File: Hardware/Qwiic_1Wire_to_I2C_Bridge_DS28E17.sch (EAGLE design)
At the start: 20 parts, among them J1 RJ45, J2 RJ45, J3 RJ11, J4 RJ11

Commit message: Update to board
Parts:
- removed JP4: JUMPER-SMT_3_NO_NO-SILK, SparkFun-Jumpers:JUMPER-SMT_3_NO_NO-SILK
- removed U$1: DS28E17, SparkX:DS28E17
- added JP6: JUMPER-SMT_2_NC_PASTE_SILK, SparkFun-Jumpers:JUMPER-SMT_2_NC_PASTE_SILK
- added LOGO1: OSHW-LOGOM, SparkFun-Aesthetics:OSHW-LOGOM
- added U$2, U$3: SPARKX-LOGO5, SparkX:SPARKX-LOGO5
- added U1: DS28E17, SparkX:DS28E17
- JP2: value JUMPER-SMT_2_NO_NO-SILK -> JUMPER-SMT_3_2-NC_PASTE_SILK; device SparkFun-Jumpers:JUMPER-SMT_2_NO_NO-SILK -> SparkFun-Jumpers:JUMPER-SMT_3_2-NC_PASTE_SILK
- R3: value 4.7K -> 4.7k; device SparkFun-Resistors:4.7KOHM-1/10W-1%(0603) -> SparkFun-Resistors:4.7KOHM-0603-1/10W-1%
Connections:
- net 3.3V: now also JP6.2, U1.VCC; no longer JP4.2, U$1.VCC
- net AWAKE: now also U1.AWAKE; no longer U$1.AWAKE
- net BUSY: now also U1.BUSY; no longer U$1.BUSY
- net ED: now also U1.ED; no longer U$1.ED
- net GND: now also U1.!SLEEP, U1.GND; no longer U$1.GND, U$1.SLEEP
- net IO: now also U1.IO, U1.WAKE; no longer U$1.IO, U$1.WAKE
- net N$1: now also U1.REG18; no longer U$1.REG18
- net N$2: now also JP6.1; no longer JP2.1
- net N$3: now also JP2.1; no longer JP4.1
- net N$4: now also JP2.3; no longer JP4.3
- net SCL: now also U1.SCL; no longer U$1.SCL
- net SDA: now also U1.SDA; no longer U$1.SDA
- net XD: now also U1.XD; no longer U$1.XD
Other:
- note added: "1WIRE PTH"
- note added: "1Wire Bus"
- note added: "DS28E17"
- note added: "I2C PTH"
- note added: "JP2 = I2C Pullups Closed by Default"
- note added: "JP6 = 1Wire Pullup Closed by Default"
- note added: "Qwiic I2C ports"
- note added: "X10"
- note removed: "1Wire - IN"
- note removed: "1Wire - OUT"
- moved on the sheet: C1, J1, J2, J3, J4, J5, JP1, JP3, JP5, R1, R2, R3

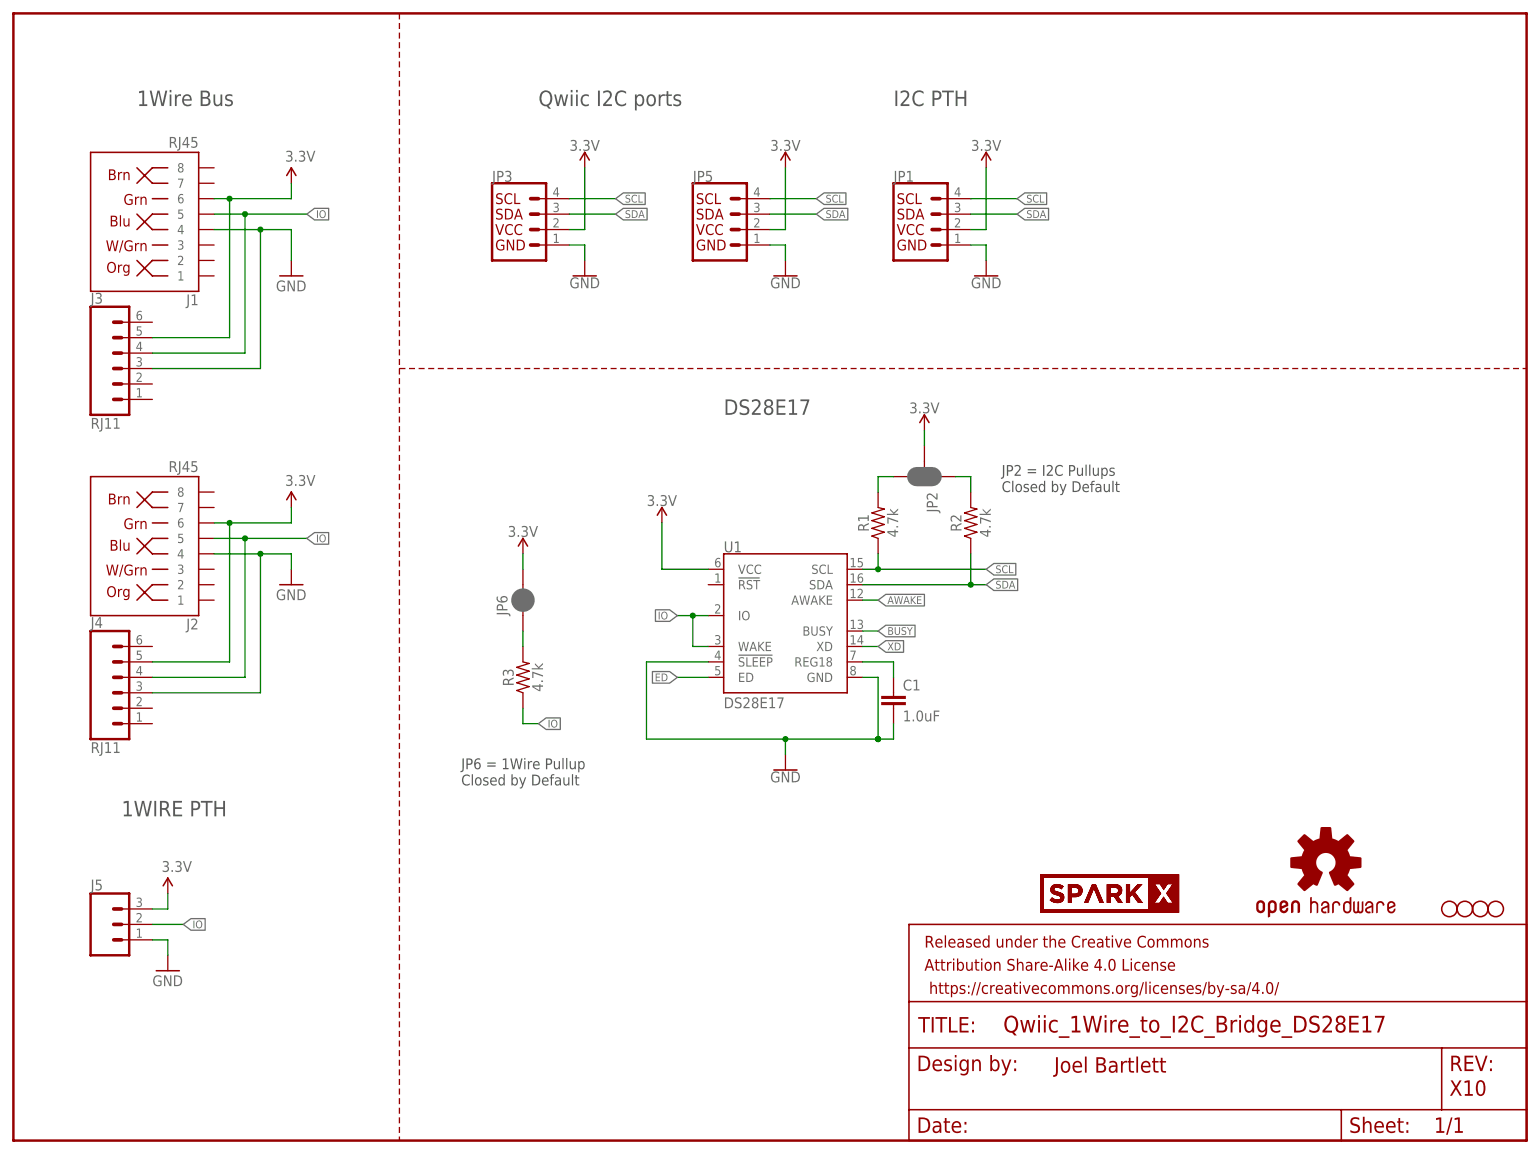
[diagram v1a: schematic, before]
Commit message: Added RJ45/RJ11 footprint. CAM new panel gerbers
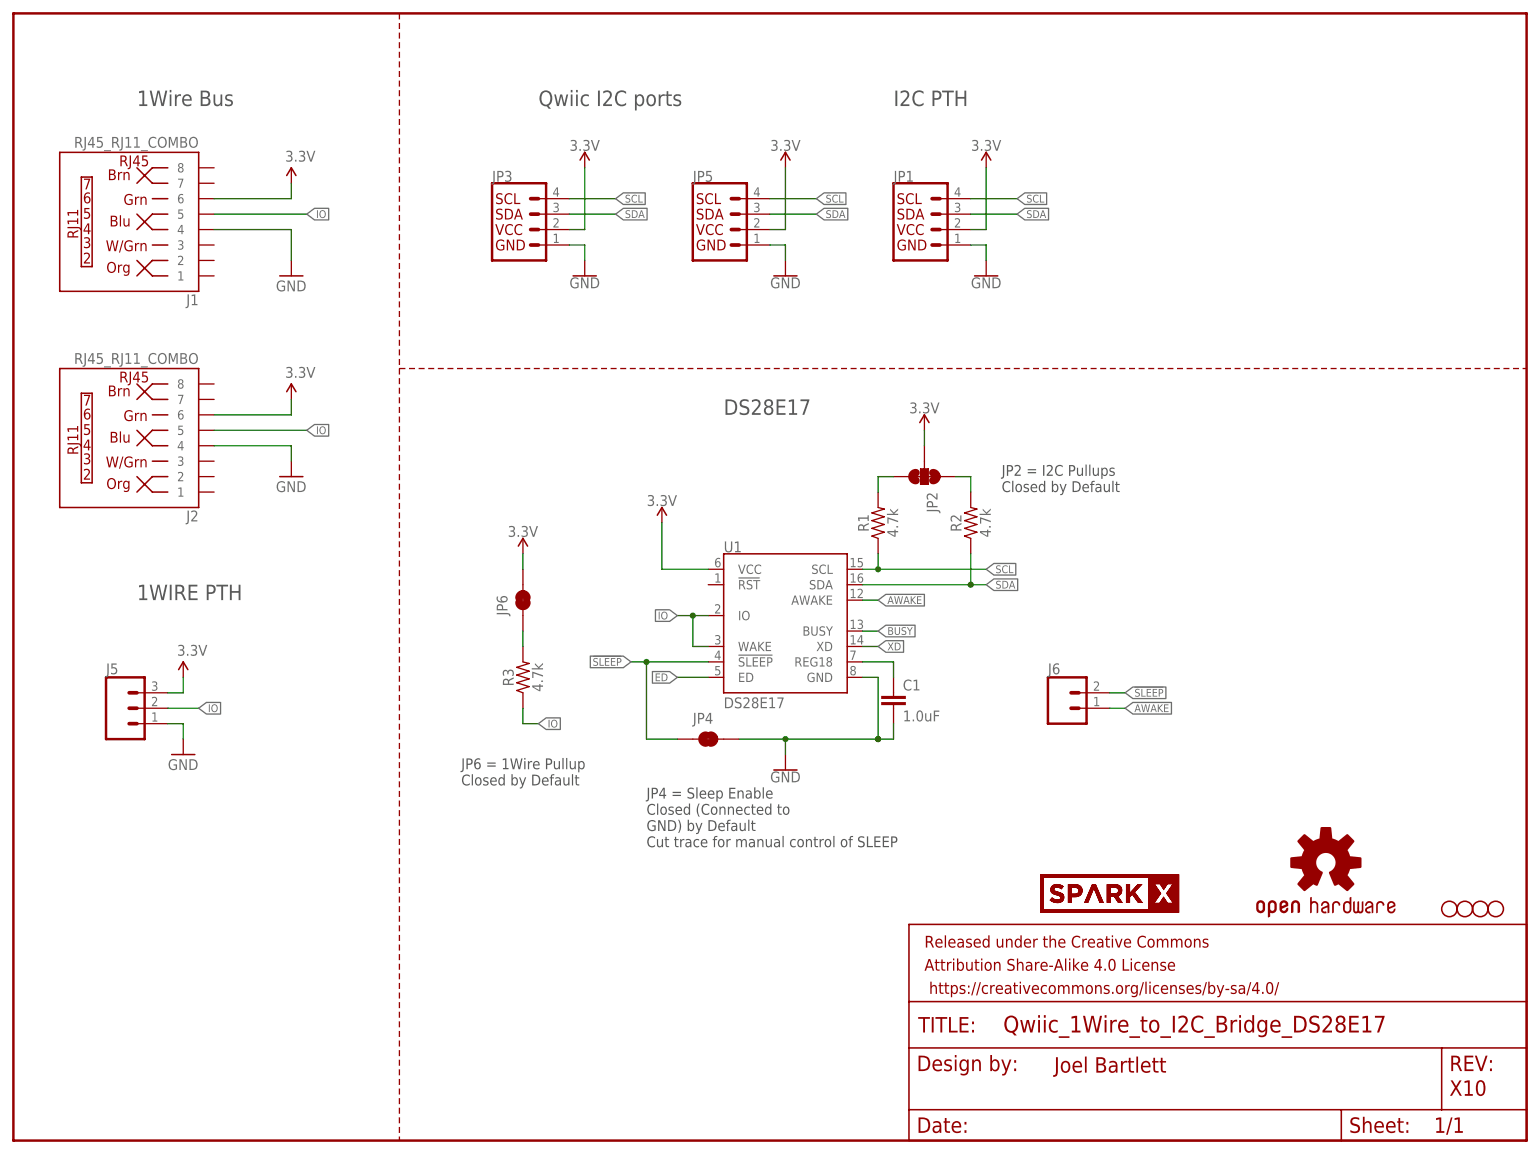
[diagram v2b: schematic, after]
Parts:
- removed J3, J4: RJ11, SparkFun-Connectors:RJ11-6
- added J6: (no value), SparkFun-Connectors:CONN_02
- added JP4: JUMPER-SMT_2_NC_TRACE_SILK, SparkFun-Jumpers:JUMPER-SMT_2_NC_TRACE_SILK
- J1, J2: value RJ45 -> RJ45_RJ11_COMBO; device SparkFun-Connectors:RJ45-8 -> SparkX:RJ45_RJ11_COMBO
- JP2: value JUMPER-SMT_3_2-NC_PASTE_SILK -> JUMPER-SMT_3_2-NC_TRACE_SILK; device SparkFun-Jumpers:JUMPER-SMT_3_2-NC_PASTE_SILK -> SparkFun-Jumpers:JUMPER-SMT_3_2-NC_TRACE_SILK
- JP6: value JUMPER-SMT_2_NC_PASTE_SILK -> JUMPER-SMT_2_NC_TRACE_SILK; device SparkFun-Jumpers:JUMPER-SMT_2_NC_PASTE_SILK -> SparkFun-Jumpers:JUMPER-SMT_2_NC_TRACE_SILK
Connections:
- new net !SLEEP: J6.2, JP4.1, U1.!SLEEP
- net 3.3V: no longer J3.5, J4.5
- net AWAKE: now also J6.1
- net GND: now also JP4.2; no longer J3.3, J4.3, U1.!SLEEP
- net IO: no longer J3.4, J4.4
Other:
- note added: "JP4 = Sleep Enable Closed (Connected to GND) by Default Cut trace for manual control of SLEEP"
- moved on the sheet: J5
